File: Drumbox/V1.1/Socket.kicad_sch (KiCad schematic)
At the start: 36 parts, among them J10 Bass OUT, J11 LBonga OUT, J12 Conn_01x04_Female, J13 Conn_01x04_Male, J14 Conn_01x04_Female, J15 Conn_01x04_Male, J16 HBonga OUT, J17 Clave OUT, J18 Conn_01x03_Female, J19 Conn_01x03_Male, J20 Main OUT, J6 Bass IN, J7 LBonga IN, J8 HBonga IN, J9 Clave IN, U2 TL074

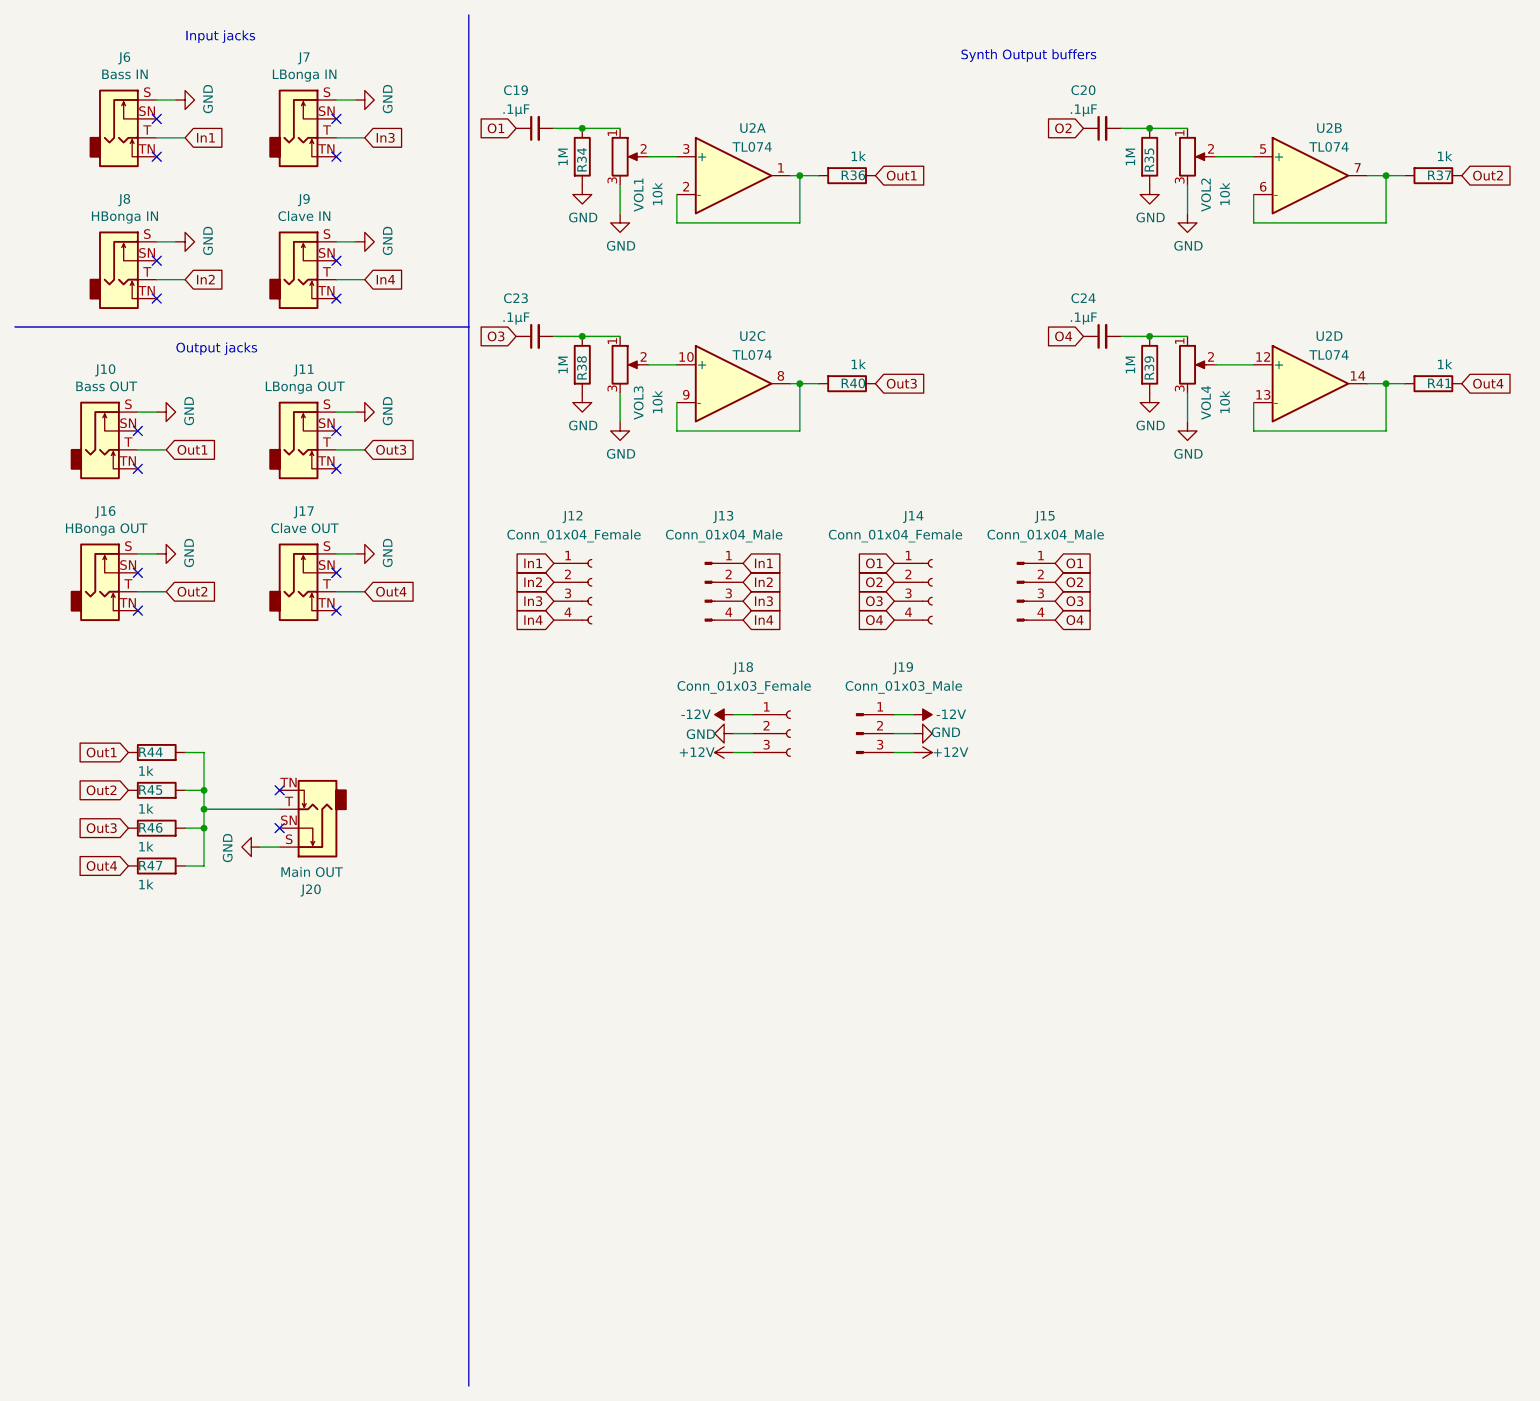
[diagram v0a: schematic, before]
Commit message: update drumbox
delete chanel output for single output + add button to trigger each sound
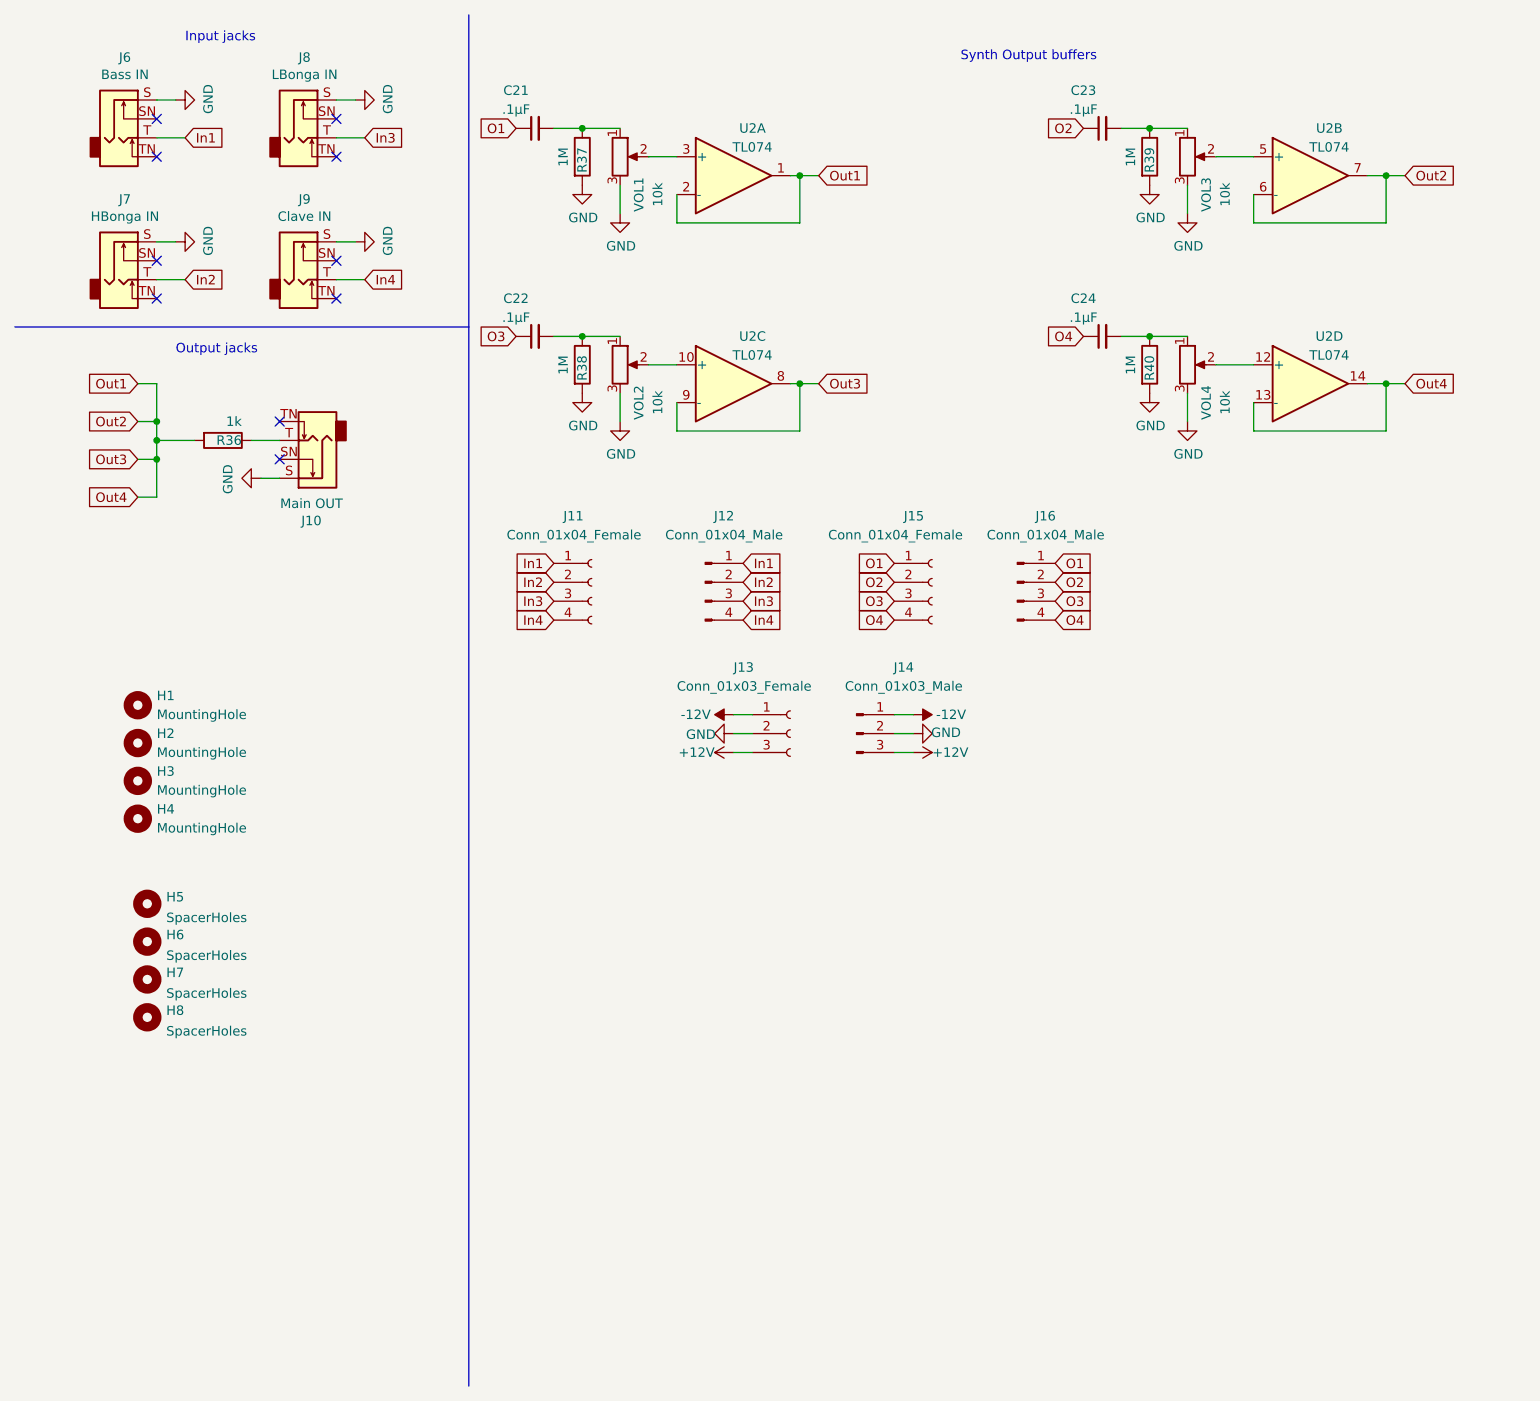
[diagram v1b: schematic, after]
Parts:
- removed J10: Bass OUT, Connector_Audio:Jack_3.5mm_QingPu_WQP-PJ398SM_Vertical_CircularHoles, symbol Connector:AudioJack2_Switch
- removed J11: LBonga OUT, Connector_Audio:Jack_3.5mm_QingPu_WQP-PJ398SM_Vertical_CircularHoles, symbol Connector:AudioJack2_Switch
- removed J16: HBonga OUT, Connector_Audio:Jack_3.5mm_QingPu_WQP-PJ398SM_Vertical_CircularHoles, symbol Connector:AudioJack2_Switch
- removed J17: Clave OUT, Connector_Audio:Jack_3.5mm_QingPu_WQP-PJ398SM_Vertical_CircularHoles, symbol Connector:AudioJack2_Switch
- removed R37, R40, R41, R44, R45, R46, R47: 1k, Resistor_THT:R_Axial_DIN0207_L6.3mm_D2.5mm_P10.16mm_Horizontal, symbol Device:R
- added H1, H2, H3, H4: MountingHole, Synth:Doepfer Mounting hole, symbol Mechanical:MountingHole
- added H5, H6, H7, H8: SpacerHoles, MountingHole:MountingHole_3.2mm_M3, symbol Mechanical:MountingHole
- renumbered C19 to C21, C23 to C22, C20 to C23, J20 to J10, J12 to J11, J13 to J12, J18 to J13, J19 to J14, J14 to J15, J15 to J16, J8 to J7, J7 to J8, R34 to R37, R35 to R39, R39 to R40, VOL3 to VOL2, VOL2 to VOL3
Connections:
- net Out1: now also R36.2, U2.1, U2.13 (-), U2.14, U2.2 (-), U2.6 (-), U2.7, U2.8, U2.9 (-); no longer R36.1
- net at J10.T: now also R36.1
- no-connect marks 18 -> 10
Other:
- moved on the sheet: J10
